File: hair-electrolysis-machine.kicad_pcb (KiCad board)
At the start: 2 copper layers, 53 x 53 mm, 80 parts, among them J1 USB_C_Receptacle_USB2.0_16P, J2 Conn_01x04_Pin, J3 AudioJack2_Ground_Switch, J4 AudioJack2_Ground_Switch, J5 Conn_01x04_Pin, J6 Conn_01x04_Pin, J7 AudioJack2_Ground_Switch, Q2 BSS138, SW3 SW_SPDT, SW4 RotaryEncoder_Switch, SW7 BTN, SW8 BTN, SW9 BTN, U1 STM32G0B1RBTx, U2 TP4054, U4 XC6206PxxxMR, U8 LM358B

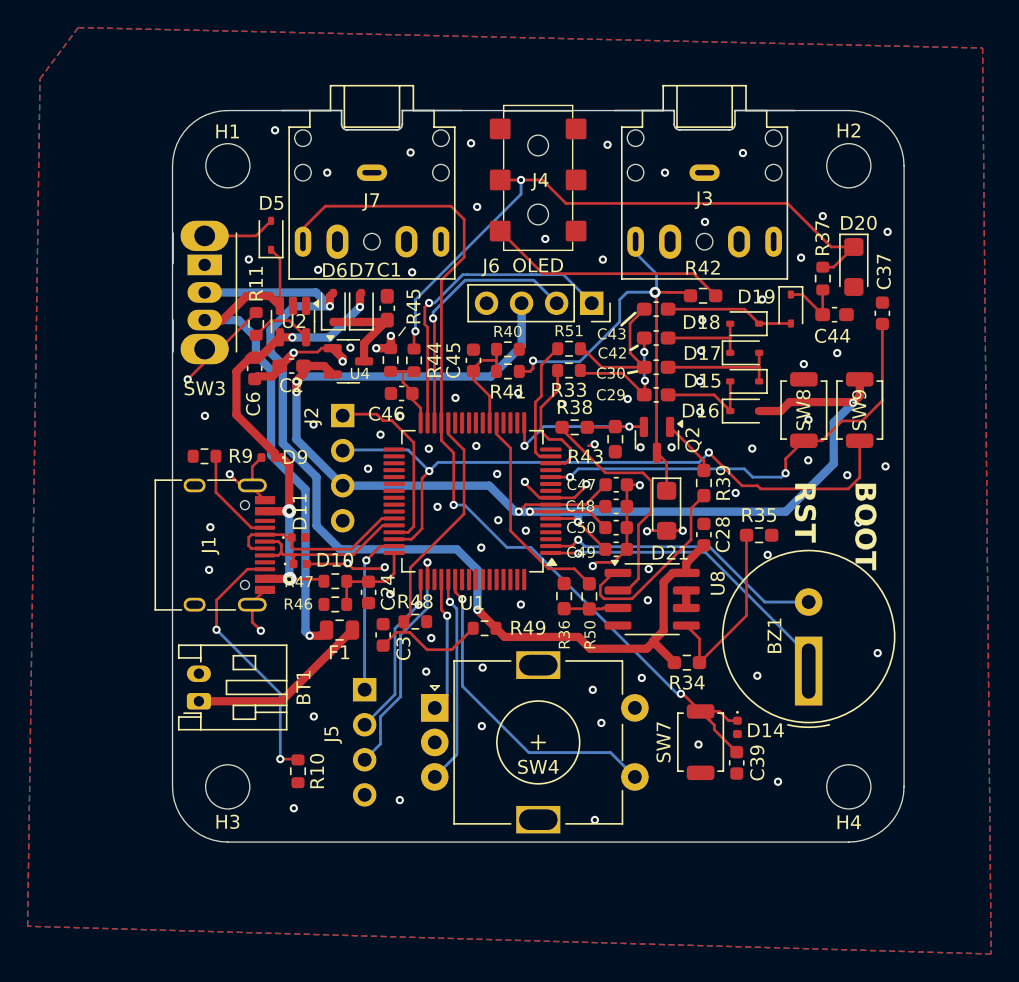
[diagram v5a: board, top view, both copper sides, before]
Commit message: Added charge indicator LED, upped charge pump capacitor bank voltage rating for more headroom
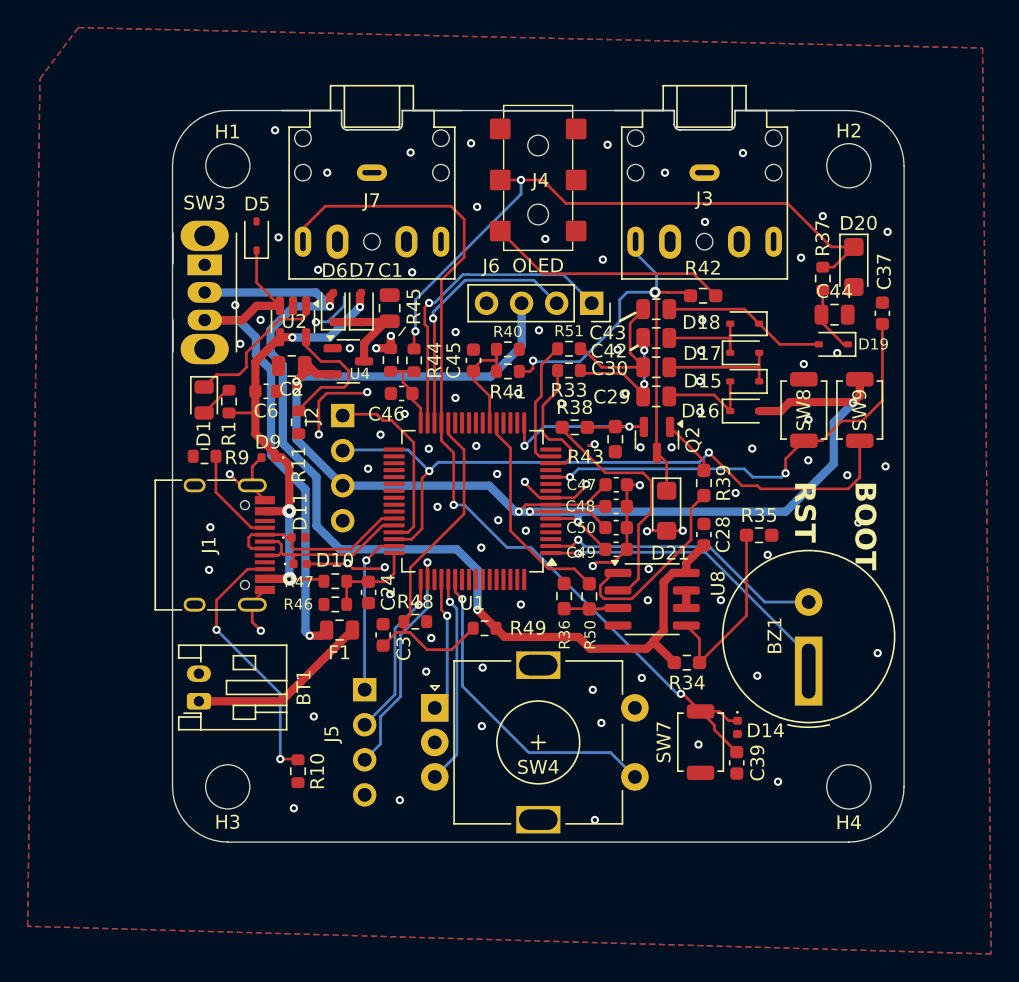
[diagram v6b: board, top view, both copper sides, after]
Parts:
- added D1: LED, LED_SMD:LED_0805_2012Metric, F.Cu at (125.3, 92.0)
- added R1: 1K, Resistor_SMD:R_0603_1608Metric, F.Cu at (127.1, 92.1)
- C1, C2, C29, C30, C42, C43, C44: footprint Capacitor_SMD:C_0603_1608Metric_Pad1.08x0.95mm_HandSolder -> Capacitor_SMD:C_0805_2012Metric
- C6: value 100nF -> 1uF
- moved R11 7.77 mm to (132.2, 93.6), turned to 90 degrees
- moved D19 4.00 mm to (170.9, 87.9), turned to 180 degrees
- moved C6 1.86 mm to (129.8, 91.3), turned to 180 degrees
- moved D5 1.05 mm to (129.1, 80.1)
- moved C1 0.17 mm to (138.7, 85.3)
- moved C29 0.11 mm to (158.0, 91.7)
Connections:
- U2 pad 1: unconnected-(U2-STAT-Pad1) -> Net-(D1-K)
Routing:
- net Net-(D1-K): track 0.00 -> 11.3 mm
- net GND: track 55.1 -> 44.4 mm, vias 88 -> 92
- net Net-(U2-PROG): track 4.90 -> 10.2 mm
- net Net-(D18-K): track 9.33 -> 12.1 mm
- net Net-(D1-A): track 0.00 -> 2.48 mm
- net /Mcu/TRIGGER: track 67.5 -> 66.5 mm

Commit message: Fixed switch mounting holes not being grounded
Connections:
- SW3 pad MP: (no net) -> GND
- SW4 pad MP: (no net) -> GND
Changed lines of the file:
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@@
 			(unit
 				(name "A")
-				(pins "2" "1" "3")
+				(pins "2" "MP" "1" "3")
 			)
 		)
@@
 			(layers "*.Cu" "*.Mask")
 			(remove_unused_layers no)
+			(net "GND")
+			(pinfunction "MP_MP")
+			(pintype "passive")
 		)
 		(pad "MP" thru_hole oval
@@
 			(layers "*.Cu" "*.Mask")
 			(remove_unused_layers no)
+			(net "GND")
+			(pinfunction "MP_MP")
+			(pintype "passive")
 		)
 		(embedded_fonts no)
@@
 		(tags "rotary encoder")
 		(property "Reference" "SW4"
-			(at 7.5 4.31 0)
+			(at 7.25 2.5 0)
 			(layer "F.SilkS")
 			(effects
@@
 			(unit
 				(name "A")
-				(pins "A" "C" "B" "S1" "S2")
+				(pins "A" "C" "B" "MP" "S1" "S2")
 			)
 		)
@@
 			(layers "*.Cu" "*.Mask")
 			(remove_unused_layers no)
+			(net "GND")
+			(pinfunction "MP_MP")
+			(pintype "passive")
 		)
 		(pad "MP" thru_hole rect
@@
 			(layers "*.Cu" "*.Mask")
 			(remove_unused_layers no)
+			(net "GND")
+			(pinfunction "MP_MP")
+			(pintype "passive")
 		)
 		(pad "S1" thru_hole circle
@@
 	)
 	(segment
+		(start 125.295 91.035)
+		(end 125.29 91.035)
+		(width 0.2)
+		(layer "F.Cu")
+		(net "Net-(D1-K)")
+	)
+	(segment
+		(start 127.82 90.14)
+		(end 128.35 89.61)
+		(width 0.2)
+		(layer "F.Cu")
+		(net "Net-(D1-K)")
+	)
+	(segment
+		(start 128.35 89.61)
+		(end 128.35 88.55)
+		(width 0.2)
+		(layer "F.Cu")
+		(net "Net-(D1-K)")
+	)
+	(segment
+		(start 130.7875 86.1125)
+		(end 132.379999 86.1125)
+		(width 0.2)
+		(layer "F.Cu")
+		(net "Net-(D1-K)")
+	)
+	(segment
+		(start 132.379999 86.1125)
+		(end 132.68 85.812499)
+		(width 0.2)
+		(layer "F.Cu")
+		(net "Net-(D1-K)")
+	)
+	(segment
+		(start 132.68 85.812499)
+		(end 132.68 85.15)
+		(width 0.2)
+		(layer "F.Cu")
+		(net "Net-(D1-K)")
+	)
+	(segment
+		(start 128.35 88.55)
+		(end 130.7875 86.1125)
+		(width 0.2)
+		(layer "F.Cu")
+		(net "Net-(D1-K)")
+	)
+	(segment
+		(start 126.185 90.14)
+		(end 127.82 90.14)
+		(width 0.2)
+		(layer "F.Cu")
+		(net "Net-(D1-K)")
+	)
+	(segment
+		(start 125.29 91.035)
+		(end 125.755 91.035)
+		(width 0.2)
+		(layer "F.Cu")
+		(net "Net-(D1-K)")
+	)
+	(segment
+		(start 125.29 91.035)
+		(end 126.185 90.14)
+		(width 0.2)
+		(layer "F.Cu")
+		(net "Net-(D1-K)")
+	)
+	(segment
+		(start 126.94 91.26)
+		(end 127.09 91.26)
+		(width 0.2)
+		(layer "F.Cu")
+		(net "Net-(D1-A)")
+	)
+	(segment
+		(start 125.29 92.91)
+		(end 126.94 91.26)
+		(width 0.2)
+		(layer "F.Cu")
+		(net "Net-(D1-A)")
+	)
+	(segment
 		(start 165.50625 90.6225)
 		(end 165.50625 89.63)
@@
 		(net "unconnected-(J3-PadS)")
 	)
-	(segment
-		(start 125.295 91.035)
-		(end 125.29 91.035)
-		(width 0.2)
-		(layer "F.Cu")
-		(net "Net-(D1-K)")
-	)
-	(segment
-		(start 127.82 90.14)
-		(end 128.35 89.61)
-		(width 0.2)
-		(layer "F.Cu")
-		(net "Net-(D1-K)")
-	)
-	(segment
-		(start 128.35 89.61)
-		(end 128.35 88.55)
-		(width 0.2)
-		(layer "F.Cu")
-		(net "Net-(D1-K)")
-	)
-	(segment
-		(start 130.7875 86.1125)
-		(end 132.379999 86.1125)
-		(width 0.2)
-		(layer "F.Cu")
-		(net "Net-(D1-K)")
-	)
-	(segment
-		(start 132.379999 86.1125)
-		(end 132.68 85.812499)
-		(width 0.2)
-		(layer "F.Cu")
-		(net "Net-(D1-K)")
-	)
-	(segment
-		(start 132.68 85.812499)
-		(end 132.68 85.15)
-		(width 0.2)
-		(layer "F.Cu")
-		(net "Net-(D1-K)")
-	)
-	(segment
-		(start 128.35 88.55)
-		(end 130.7875 86.1125)
-		(width 0.2)
-		(layer "F.Cu")
-		(net "Net-(D1-K)")
-	)
-	(segment
-		(start 126.185 90.14)
-		(end 127.82 90.14)
-		(width 0.2)
-		(layer "F.Cu")
-		(net "Net-(D1-K)")
-	)
-	(segment
-		(start 125.29 91.035)
-		(end 125.755 91.035)
-		(width 0.2)
-		(layer "F.Cu")
-		(net "Net-(D1-K)")
-	)
-	(segment
-		(start 125.29 91.035)
-		(end 126.185 90.14)
-		(width 0.2)
-		(layer "F.Cu")
-		(net "Net-(D1-K)")
-	)
-	(segment
-		(start 126.94 91.26)
-		(end 127.09 91.26)
-		(width 0.2)
-		(layer "F.Cu")
-		(net "Net-(D1-A)")
-	)
-	(segment
-		(start 125.29 92.91)
-		(end 126.94 91.26)
-		(width 0.2)
-		(layer "F.Cu")
-		(net "Net-(D1-A)")
-	)
 	(zone

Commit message: Some minor clean ups
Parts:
- renumbered C6 to C1, C30 to C10, C37 to C11, C45 to C12, C42 to C13, C43 to C14, C46 to C15, C39 to C16, C44 to C17, C24 to C18, C3 to C19, C1 to C2, C2 to C3, C28 to C4, C50 to C5, C48 to C6, C49 to C7, C47 to C8, C29 to C9, D11 to D10, D10 to D11, D18 to D12, D19 to D13, D20 to D15, D5 to D2, D7 to D3, D6 to D4, D21 to D5, D15 to D6, D16 to D7, D17 to D8, J5 to J1, J1 to J2, J7 to J3, J6 to J4, J2 to J5, J3 to J6, J4 to J7, Q2 to Q1, R11 to R1, R51 to R10, R33 to R11, R40 to R12, R41 to R13, R9 to R14, R10 to R15, R44 to R16, R45 to R17, R37 to R18, R42 to R19, R1 to R2, R47 to R20, R46 to R21, R49 to R22, R48 to R23, R34 to R3, R35 to R4, R50 to R5, R36 to R6, R38 to R7, R39 to R8, R43 to R9, SW3 to SW1, SW8 to SW2, SW9 to SW3, SW7 to SW5, U2 to U1, U4 to U2, U8 to U3, U1 to U4
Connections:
- J6 pad R: unconnected-(J3-PadR) -> /Mcu/FOLLICLE_ELECTRODE
- J6 pad S: unconnected-(J3-PadS) -> /Mcu/FOLLICLE_ELECTRODE
- J7 pad R: unconnected-(J4-PadR) -> /Mcu/BODY_ELECTRODE
- J7 pad S: unconnected-(J4-PadS) -> /Mcu/BODY_ELECTRODE
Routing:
- net /Mcu/FOLLICLE_ELECTRODE: track 36.2 -> 55.2 mm
- net GND: track 44.4 -> 50.8 mm
- net /Mcu/BODY_ELECTRODE: track 45.9 -> 51.0 mm
- net unconnected-(J3-PadR): track 2.40 -> 0.00 mm
- net unconnected-(J3-PadS): track 0.88 -> 0.00 mm
- net /Mcu/I2C2_SDA: track 22.4 -> 21.6 mm
